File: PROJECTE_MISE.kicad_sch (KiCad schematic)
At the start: 48 parts, among them IC1 MSP430FR2355TPT, J1 conn_DFrobot, J10 SDA_{TP}, J11 SCL_{TP}, J12 SCL_{TP-GND}, J13 SPI_{TP-MISO}, J14 SPI_{TP-SS}, J15 SPI_{TP-SCLK}, J16 SPI_{TP-MOSI}, J17 SPI_{TP-GND}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

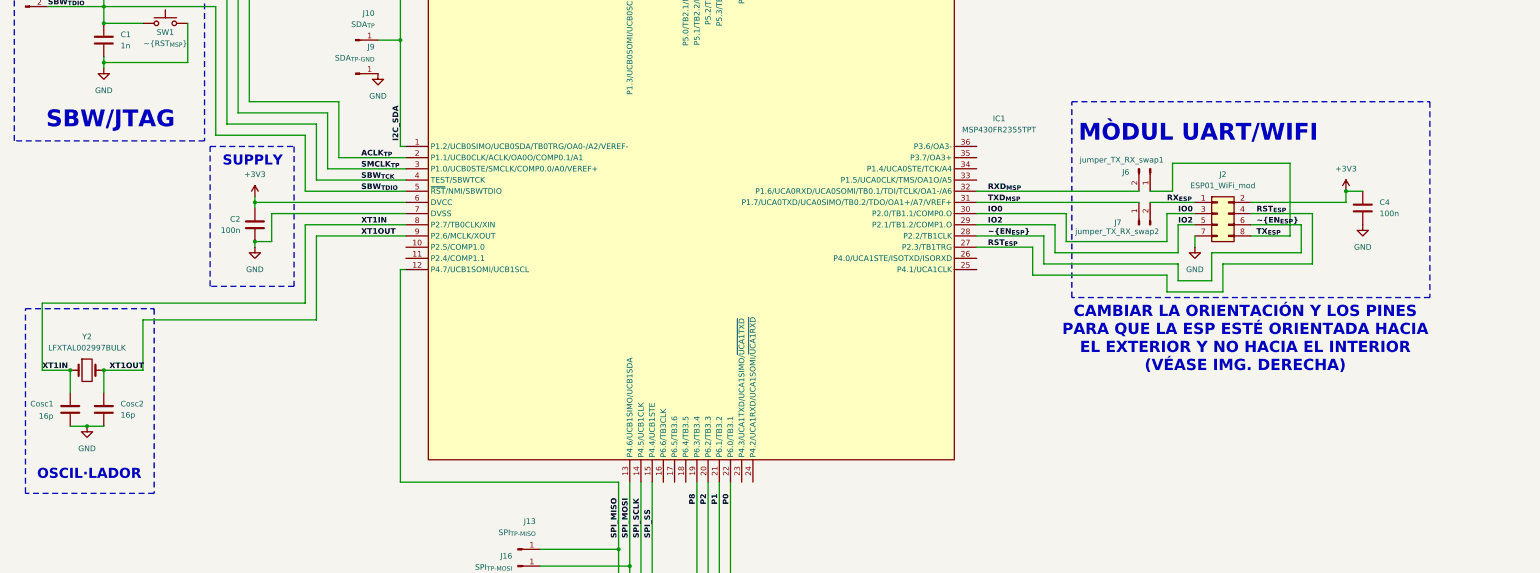
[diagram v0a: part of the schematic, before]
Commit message: modul wifi girat
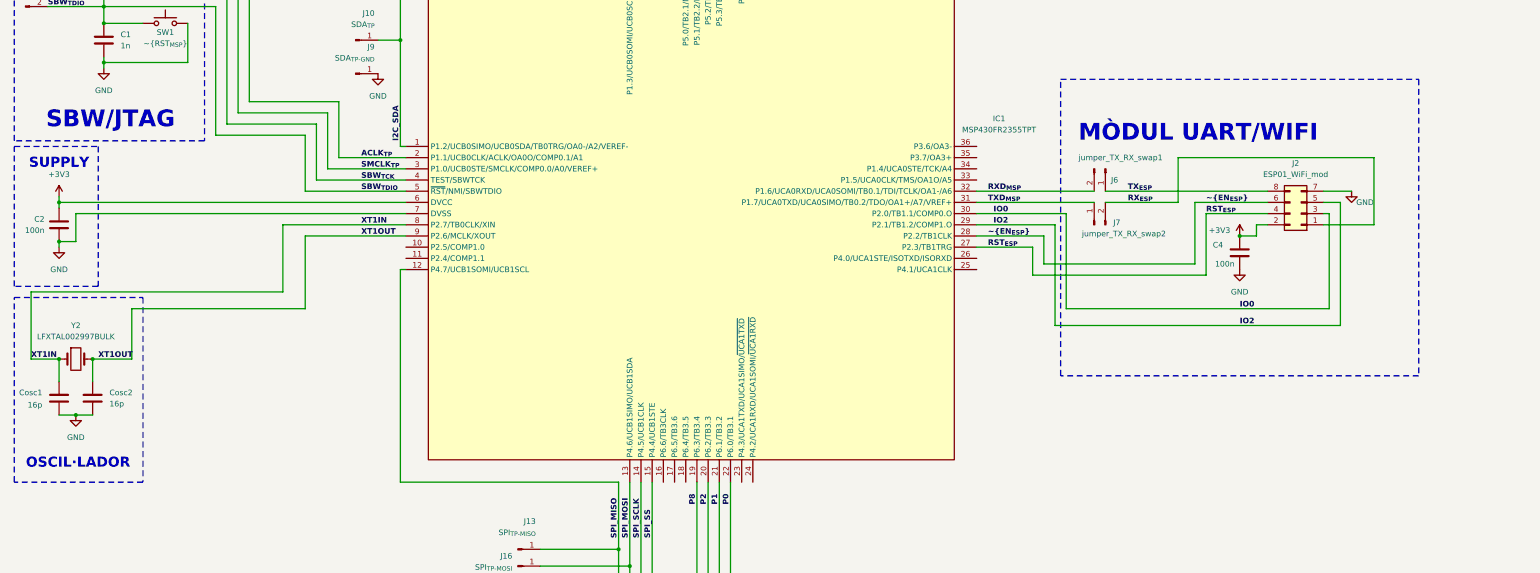
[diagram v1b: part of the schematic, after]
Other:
- note removed: "CAMBIAR LA ORIENTACIÓN Y LOS PINES PARA QUE LA ESP ESTÉ ORIENTADA HACIA EL EXTERIOR Y NO HACIA EL INTERIOR (VÉASE IMG. DERECHA)"
- moved on the sheet: C2, C4, Cosc1, Cosc2, J2, J6, J7, Y2

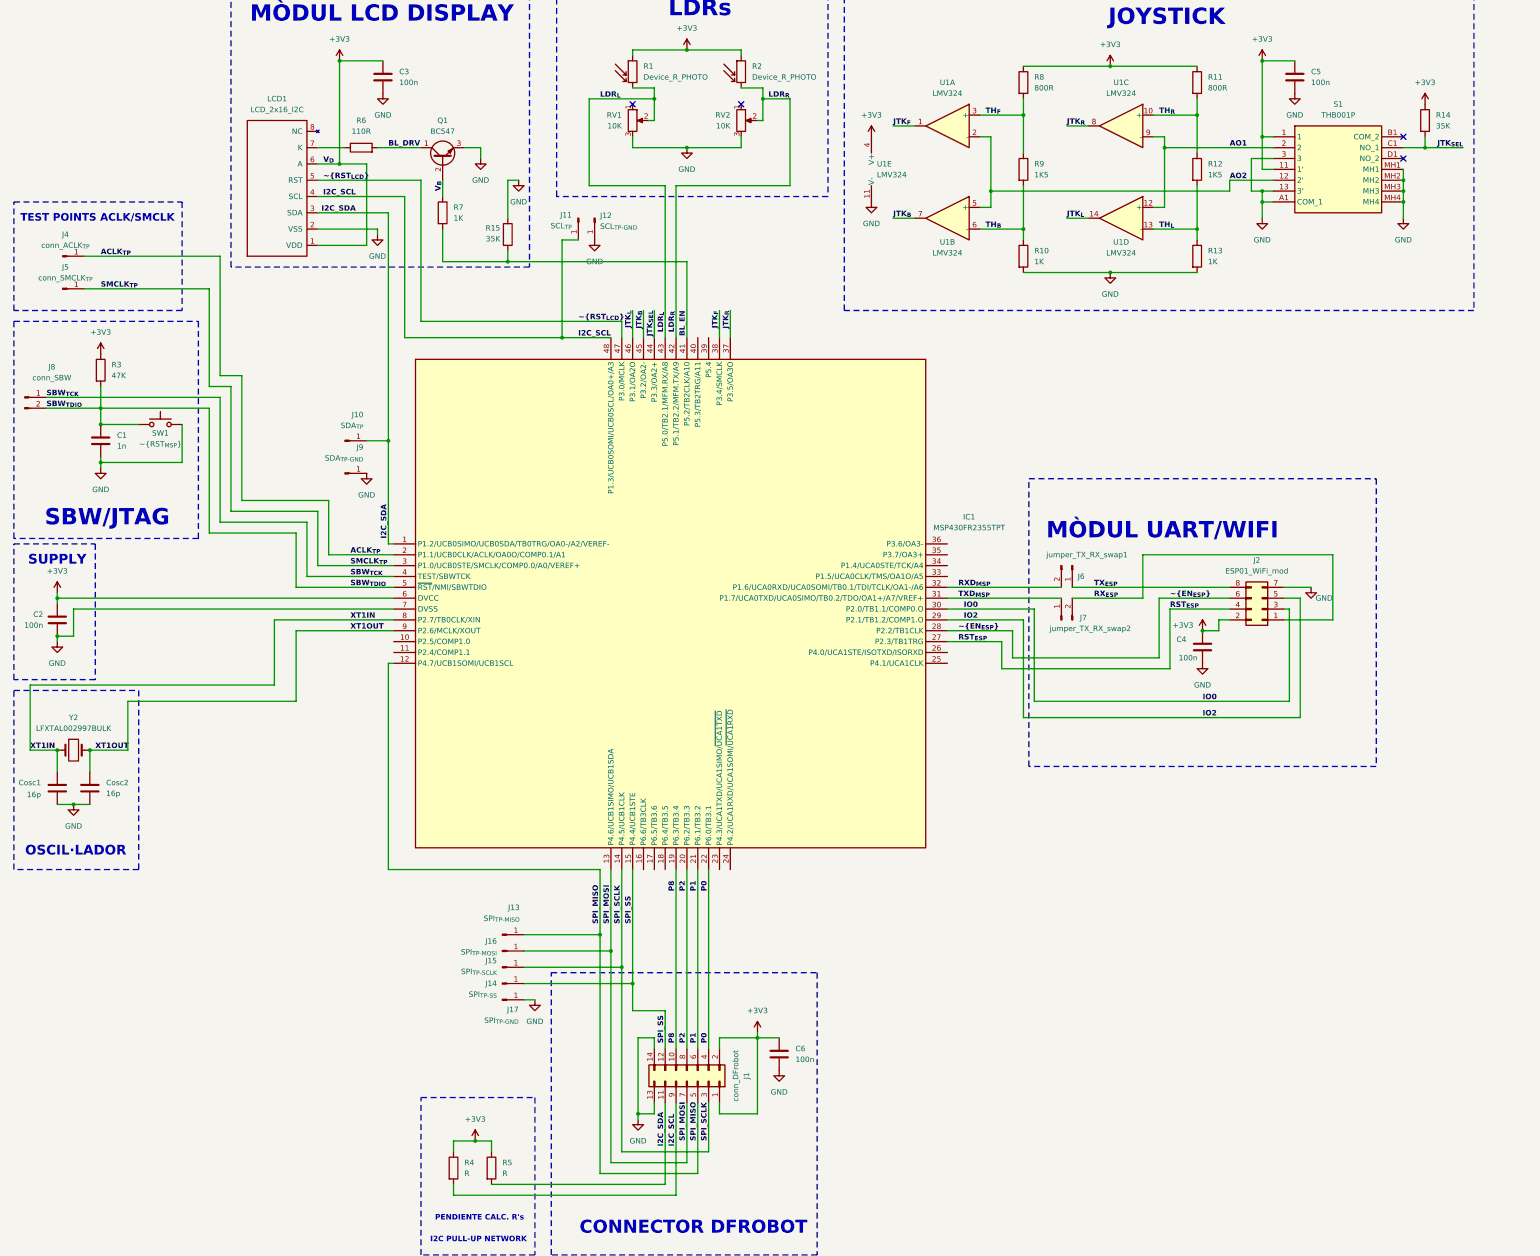
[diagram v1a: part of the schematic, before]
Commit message: updated wifi & crystal
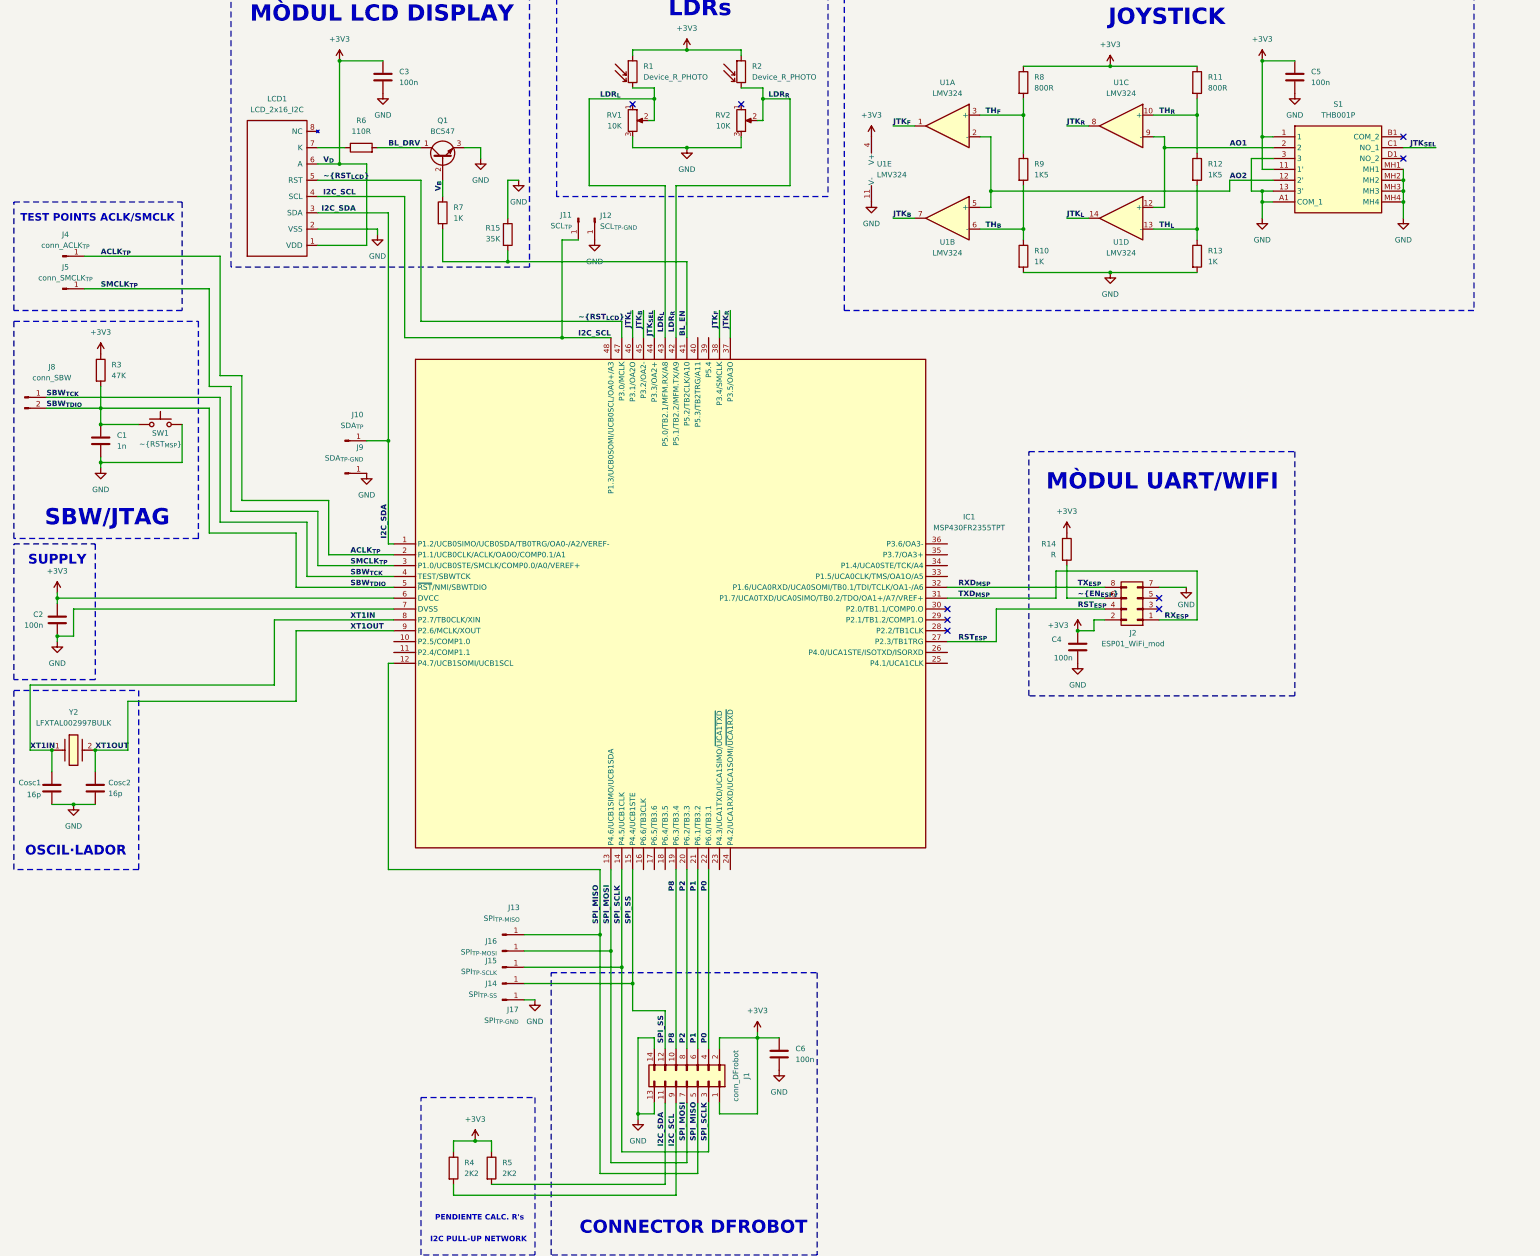
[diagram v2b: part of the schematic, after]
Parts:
- removed J6: jumper_TX_RX_swap1, symbol Connector:Conn_01x02_Pin
- removed J7: jumper_TX_RX_swap2, symbol Connector:Conn_01x02_Pin
- R14: value 35K -> R
- R4, R5: value R -> 2K2
- Y2: footprint (none) -> LFXTAL002997Bulk; symbol Device:Crystal -> LFXTAL002997Bulk:LFXTAL002997Bulk; Height (none) -> 6.2; Manufacturer_Name (none) -> IQD; Manufacturer_Part_Number (none) -> LFXTAL002997Bulk; Mouser Part Number (none) -> 449-LFXTAL002997BULK; Mouser Price/Stock (none) -> https://www.mouser.co.uk/ProductDetail/IQD/LFXTAL002997Bulk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
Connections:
- net TXD_{MSP} is gone; now on net RX_{ESP}: IC1.31 (P1.7/UCA0TXD/UCA0SIMO/TB0.2/TDO/OA1+/A7/VREF+)
- net TX_{ESP} is gone; now on net RXD_{MSP}: J2.8 (Pin_8)
- net JTK_{SEL}: no longer R14.2
- net ~{EN_{ESP}}: now also R14.2; no longer IC1.28 (P2.2/TB1CLK)
- net IO0: no longer names the net of J2.3 (Pin_3)
- net IO0: no longer IC1.30 (P2.0/TB1.1/COMP0.O)
- net IO2: no longer names the net of J2.5 (Pin_5)
- net IO2: no longer IC1.29 (P2.1/TB1.2/COMP1.O)
- no-connect marks 4 -> 9
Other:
- moved on the sheet: C4, Cosc1, Cosc2, J2

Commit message: huellas
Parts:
- C1, C2, C3, C4, C5, C6, Cosc1, Cosc2: footprint (none) -> Capacitor_SMD:C_0805_2012Metric
- J10, J11, J12, J13, J14, J15, J16, J17, J4, J5, J9: footprint (none) -> Connector_PinHeader_1.00mm:PinHeader_1x01_P1.00mm_Vertical
- J2, LCD1: footprint (none) -> Connector_PinSocket_2.54mm:PinSocket_2x04_P2.54mm_Vertical
- J8: footprint (none) -> Connector:FanPinHeader_1x03_P2.54mm_Vertical
- R10, R11, R12, R13, R14, R15, R3, R4, R5, R6, R7, R8, R9: footprint (none) -> Resistor_SMD:R_0805_2012Metric
- S1: footprint THB001P -> MiSE:THB001P
- U1: footprint (none) -> Package_SO:SOIC-14_3.9x8.7mm_P1.27mm
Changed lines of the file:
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@@
 			)
 		)
-		(property "Footprint" ""
+		(property "Footprint" "Capacitor_SMD:C_0805_2012Metric"
 			(at 131.7752 238.76 0)
 			(effects
@@
 			)
 		)
-		(property "Footprint" ""
+		(property "Footprint" "Capacitor_SMD:C_0805_2012Metric"
 			(at 300.6852 340.36 0)
 			(effects
@@
 			)
 		)
-		(property "Footprint" ""
+		(property "Footprint" "Resistor_SMD:R_0805_2012Metric"
 			(at 395.732 109.22 90)
 			(effects
@@
 			)
 		)
-		(property "Footprint" ""
+		(property "Footprint" "Connector_PinSocket_2.54mm:PinSocket_2x04_P2.54mm_Vertical"
 			(at 383.54 232.41 0)
 			(effects
@@
 			)
 		)
-		(property "Footprint" ""
+		(property "Footprint" "Capacitor_SMD:C_0805_2012Metric"
 			(at 140.6652 278.13 0)
 			(effects
@@
 			)
 		)
-		(property "Footprint" ""
+		(property "Footprint" "Resistor_SMD:R_0805_2012Metric"
 			(at 219.202 139.7 90)
 			(effects
@@
 			)
 		)
-		(property "Footprint" ""
+		(property "Footprint" "Connector_PinHeader_1.00mm:PinHeader_1x01_P1.00mm_Vertical"
 			(at 234.95 323.85 0)
 			(effects
@@
 			)
 		)
-		(property "Footprint" ""
+		(property "Footprint" "Resistor_SMD:R_0805_2012Metric"
 			(at 365.252 218.44 90)
 			(effects
@@
 			)
 		)
-		(property "Footprint" ""
+		(property "Footprint" "Connector_PinHeader_1.00mm:PinHeader_1x01_P1.00mm_Vertical"
 			(at 256.54 140.97 0)
 			(effects
@@
 			)
 		)
-		(property "Footprint" ""
+		(property "Footprint" "Connector_PinHeader_1.00mm:PinHeader_1x01_P1.00mm_Vertical"
 			(at 198.12 200.66 0)
 			(effects
@@
 			)
 		)
-		(property "Footprint" ""
+		(property "Footprint" "Connector_PinHeader_1.00mm:PinHeader_1x01_P1.00mm_Vertical"
 			(at 234.95 320.04 0)
 			(effects
@@
 			)
 		)
-		(property "Footprint" ""
+		(property "Footprint" "Connector_PinHeader_1.00mm:PinHeader_1x01_P1.00mm_Vertical"
 			(at 234.95 312.42 0)
 			(effects
@@
 			)
 		)
-		(property "Footprint" ""
+		(property "Footprint" "Package_SO:SOIC-14_3.9x8.7mm_P1.27mm"
 			(at 340.36 138.43 0)
 			(effects
@@
 			)
 		)
-		(property "Footprint" ""
+		(property "Footprint" "Resistor_SMD:R_0805_2012Metric"
 			(at 230.632 363.22 90)
 			(effects
@@
 			)
 		)
-		(property "Footprint" ""
+		(property "Footprint" "Resistor_SMD:R_0805_2012Metric"
 			(at 234.442 144.78 90)
 			(effects
@@
 			)
 		)
-		(property "Footprint" ""
+		(property "Footprint" "Capacitor_SMD:C_0805_2012Metric"
 			(at 130.5052 278.13 0)
 			(effects
@@
 			)
 		)
-		(property "Footprint" ""
+		(property "Footprint" "Resistor_SMD:R_0805_2012Metric"
 			(at 395.732 129.54 90)
 			(effects
@@
 			)
 		)
-		(property "Footprint" ""
+		(property "Footprint" "Connector_PinHeader_1.00mm:PinHeader_1x01_P1.00mm_Vertical"
 			(at 198.12 193.04 0)
 			(effects
@@
 			)
 		)
-		(property "Footprint" ""
+		(property "Footprint" "Package_SO:SOIC-14_3.9x8.7mm_P1.27mm"
 			(at 340.36 116.84 0)
 			(effects
@@
 			)
 		)
-		(property "Footprint" ""
+		(property "Footprint" "Connector_PinSocket_2.54mm:PinSocket_2x04_P2.54mm_Vertical"
 			(at 168.91 137.16 0)
 			(effects
@@
 			)
 		)
-		(property "Footprint" ""
+		(property "Footprint" "Connector_PinHeader_1.00mm:PinHeader_1x01_P1.00mm_Vertical"
 			(at 252.73 140.97 0)
 			(effects
@@
 			)
 		)
-		(property "Footprint" "THB001P"
+		(property "Footprint" "MiSE:THB001P"
 			(at 441.96 216.84 0)
 			(effects
@@
 			)
 		)
-		(property "Footprint" ""
+		(property "Footprint" "Connector_PinHeader_1.00mm:PinHeader_1x01_P1.00mm_Vertical"
 			(at 234.95 316.23 0)
 			(effects
@@
 			)
 		)
-		(property "Footprint" ""
+		(property "Footprint" "Package_SO:SOIC-14_3.9x8.7mm_P1.27mm"
 			(at 381 116.84 0)
 			(effects
@@
 			)
 		)
-		(property "Footprint" ""
+		(property "Footprint" "Resistor_SMD:R_0805_2012Metric"
 			(at 355.092 109.22 90)
 			(effects
@@
 			)
 		)
-		(property "Footprint" ""
+		(property "Footprint" "Connector:FanPinHeader_1x03_P2.54mm_Vertical"
 			(at 123.19 182.88 0)
 			(effects
@@
 			)
 		)
-		(property "Footprint" ""
+		(property "Footprint" "Capacitor_SMD:C_0805_2012Metric"
 			(at 421.3352 111.76 0)
 			(effects
@@
 			)
 		)
-		(property "Footprint" ""
+		(property "Footprint" "Resistor_SMD:R_0805_2012Metric"
 			(at 221.742 363.22 90)
 			(effects
@@
 			)
 		)
-		(property "Footprint" ""
+		(property "Footprint" "Connector_PinHeader_1.00mm:PinHeader_1x01_P1.00mm_Vertical"
 			(at 132.08 149.86 0)
 			(effects
@@
 			)
 		)
-		(property "Footprint" ""
+		(property "Footprint" "Resistor_SMD:R_0805_2012Metric"
 			(at 355.092 149.86 90)
 			(effects
@@
 			)
 		)
-		(property "Footprint" ""
+		(property "Footprint" "Capacitor_SMD:C_0805_2012Metric"
 			(at 207.9752 111.76 0)
 			(effects
@@
 			)
 		)
-		(property "Footprint" ""
+		(property "Footprint" "Package_SO:SOIC-14_3.9x8.7mm_P1.27mm"
 			(at 381 138.43 0)
 			(effects
@@
 			)
 		)
-		(property "Footprint" ""
+		(property "Footprint" "Resistor_SMD:R_0805_2012Metric"
 			(at 395.732 149.86 90)
 			(effects
@@
 			)
 		)
-		(property "Footprint" ""
+		(property "Footprint" "Capacitor_SMD:C_0805_2012Metric"
 			(at 141.9352 196.85 0)
 			(effects
@@
 			)
 		)
-		(property "Footprint" ""
+		(property "Footprint" "Package_SO:SOIC-14_3.9x8.7mm_P1.27mm"
 			(at 322.58 127 0)
 			(effects
@@
 			)
 		)
-		(property "Footprint" ""
+		(property "Footprint" "Resistor_SMD:R_0805_2012Metric"
 			(at 139.192 176.53 90)
 			(effects
@@
 			)
 		)
-		(property "Footprint" ""
+		(property "Footprint" "Resistor_SMD:R_0805_2012Metric"
 			(at 201.93 126.238 90)
 			(effects
@@
 			)
 		)
-		(property "Footprint" ""
+		(property "Footprint" "Connector_PinHeader_1.00mm:PinHeader_1x01_P1.00mm_Vertical"
 			(at 132.08 157.48 0)
 			(effects
@@
 			)
 		)
-		(property "Footprint" ""
+		(property "Footprint" "Capacitor_SMD:C_0805_2012Metric"
 			(at 370.5352 245.11 0)
 			(effects
@@
 			)
 		)
-		(property "Footprint" ""
+		(property "Footprint" "Connector_PinHeader_1.00mm:PinHeader_1x01_P1.00mm_Vertical"
 			(at 234.95 308.61 0)
 			(effects
@@
 			)
 		)
-		(property "Footprint" ""
+		(property "Footprint" "Resistor_SMD:R_0805_2012Metric"
 			(at 355.092 129.54 90)
 			(effects

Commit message: huellas_complet
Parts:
- SW1: footprint (none) -> Button_Switch_THT:SW_PUSH_6mm
- Y2: footprint LFXTAL002997Bulk -> KiCad:LFXTAL002997Bulk
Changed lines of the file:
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@@
 			)
 		)
-		(property "Footprint" ""
+		(property "Footprint" "Button_Switch_THT:SW_PUSH_6mm"
 			(at 154.94 184.15 0)
 			(effects
@@
 			)
 		)
-		(property "Footprint" "LFXTAL002997Bulk"
+		(property "Footprint" "KiCad:LFXTAL002997Bulk"
 			(at 138.43 361.62 0)
 			(effects
